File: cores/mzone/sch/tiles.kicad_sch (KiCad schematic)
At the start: 37 parts

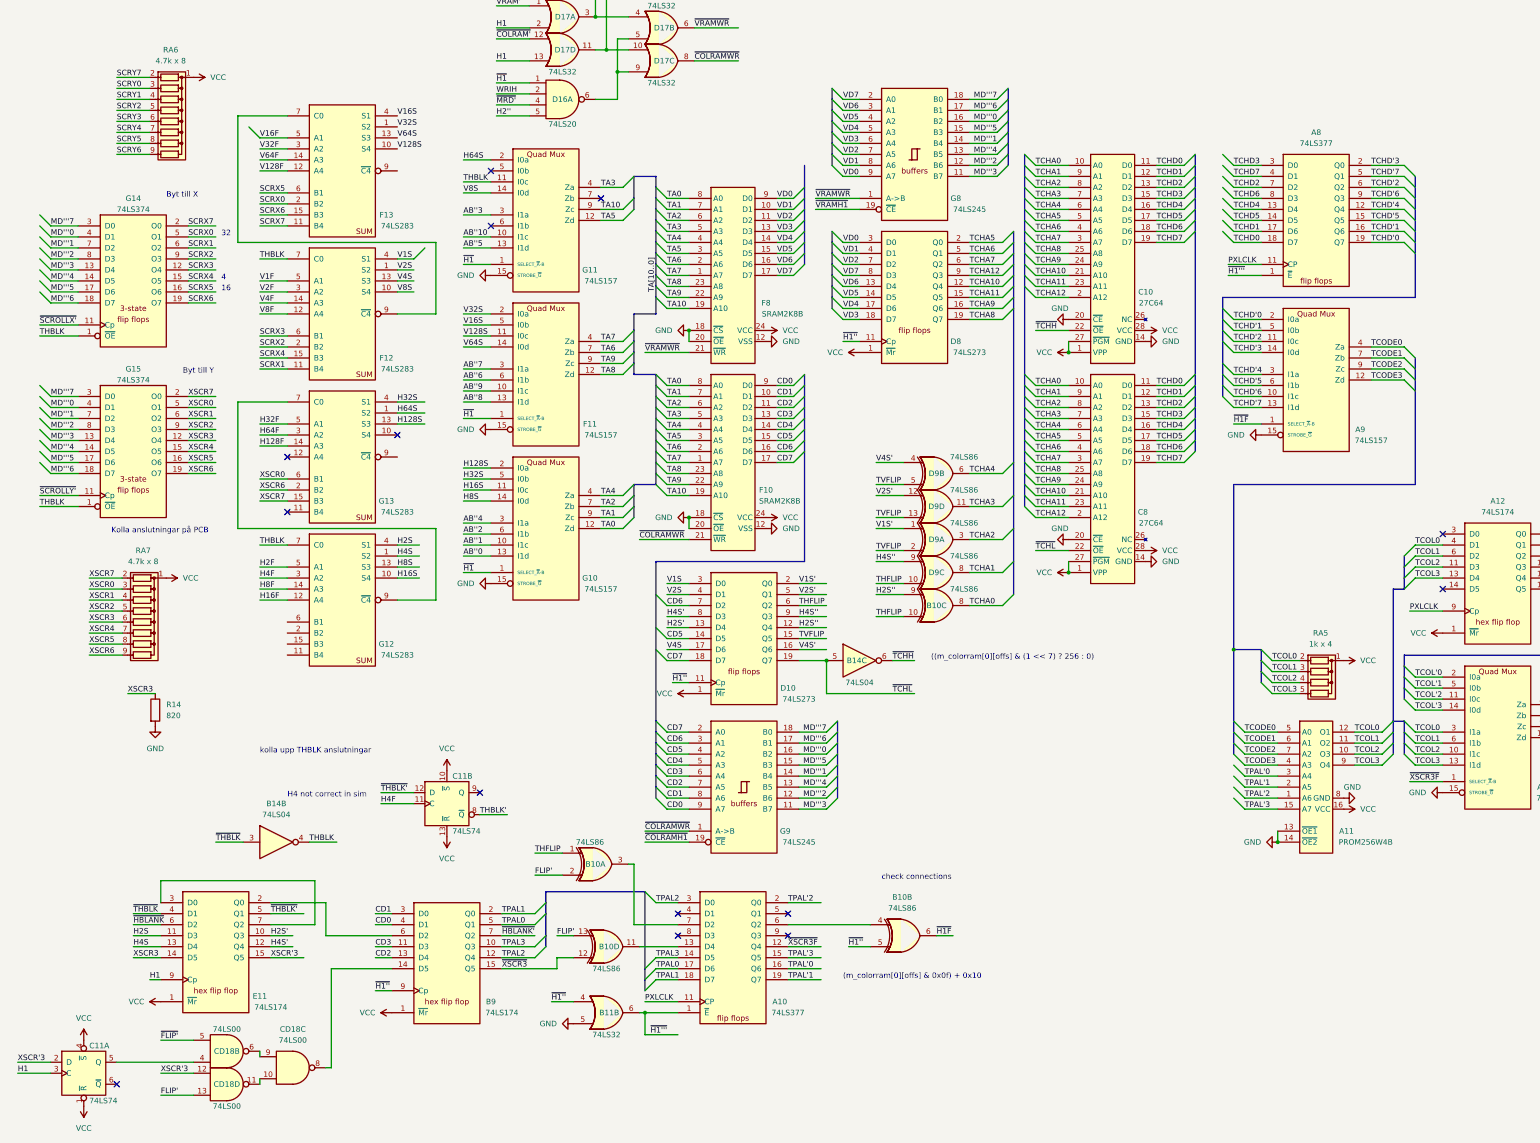
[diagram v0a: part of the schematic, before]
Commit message: mzone sim working, no sound.
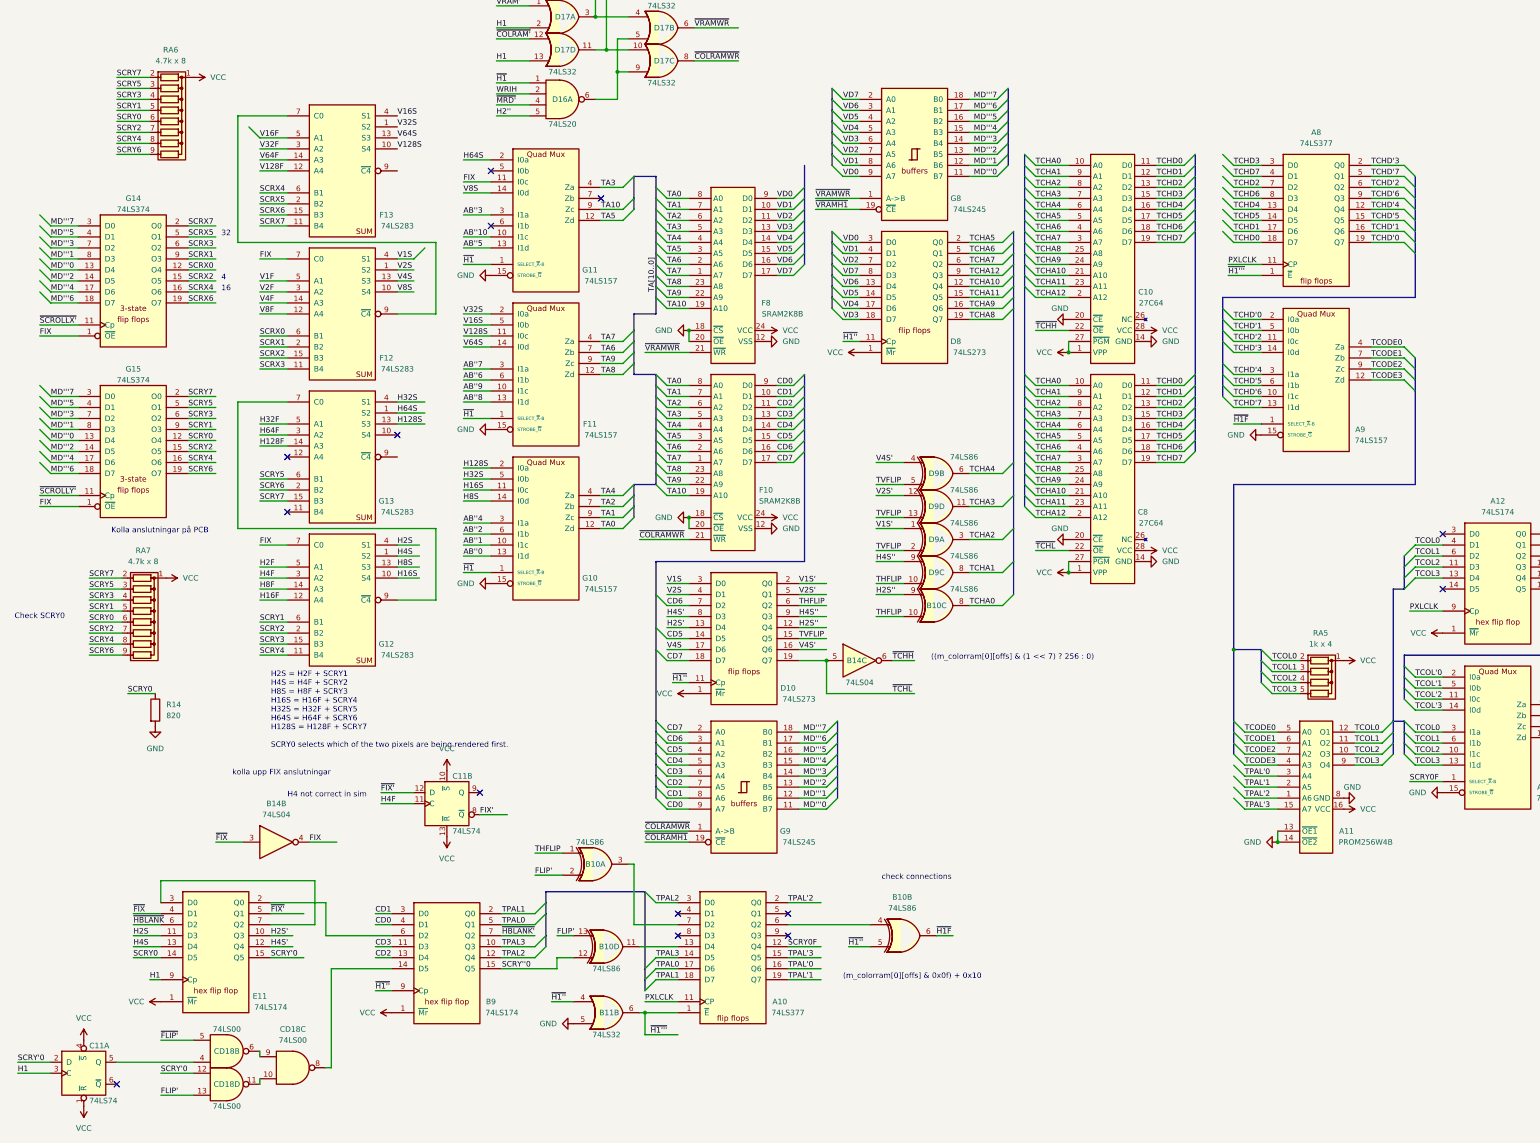
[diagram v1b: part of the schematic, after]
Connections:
- net XSCR0 is gone; now on net SCRY5: G13.6 (B1), G15.5 (O1), RA7.3 (R2)
- net XSCR1 is gone; now on net SCRY3: G15.6 (O2), RA7.4 (R3)
- net XSCR2 is gone; now on net SCRY1: G15.9 (O3), RA7.5 (R4)
- net XSCR3 is gone; now on net SCRY0: E11.14 (D5), G15.12 (O4), R14.1, RA7.6 (R5)
- net XSCR4 is gone; now on net SCRY2: G15.15 (O5), RA7.7 (R6)
- net XSCR5 is gone; now on net SCRY4: G15.16 (O6), RA7.8 (R7)
- net XSCR6 is gone; now on net SCRY6: G13.2 (B2), G15.19 (O7), RA7.9 (R8)
- net XSCR7 is gone; now on net SCRY7: G13.15 (B3), G15.2 (O0), RA7.2 (R1)
- net MD'''0: now also G14.13 (D4), G15.13 (D4), G8.11 (B7), G9.11 (B7); no longer G14.4 (D1), G15.4 (D1), G8.16 (B2), G9.16 (B2)
- net MD'''1: now also G14.8 (D3), G15.8 (D3), G8.12 (B6), G9.12 (B6); no longer G14.7 (D2), G15.7 (D2), G8.14 (B4), G9.14 (B4)
- net MD'''2: now also G14.14 (D5), G15.14 (D5), G8.13 (B5), G9.13 (B5); no longer G14.8 (D3), G15.8 (D3), G8.12 (B6), G9.12 (B6)
- net MD'''3: now also G14.7 (D2), G15.7 (D2), G8.14 (B4), G9.14 (B4); no longer G14.13 (D4), G15.13 (D4), G8.11 (B7), G9.11 (B7)
- net MD'''4: now also G14.17 (D6), G15.17 (D6), G8.15 (B3), G9.15 (B3); no longer G14.14 (D5), G15.14 (D5), G8.13 (B5), G9.13 (B5)
- net MD'''5: now also G14.4 (D1), G15.4 (D1), G8.16 (B2), G9.16 (B2); no longer G14.17 (D6), G15.17 (D6), G8.15 (B3), G9.15 (B3)
- net SCRX0: now also F12.6 (B1), G14.12 (O4); no longer F13.2 (B2), G14.5 (O1)
- net SCRX1: now also F12.2 (B2), G14.9 (O3); no longer F12.11 (B4), G14.6 (O2)
- net SCRX2: now also F12.15 (B3), G14.15 (O5); no longer F12.2 (B2), G14.9 (O3)
- net SCRX3: now also F12.11 (B4), G14.6 (O2); no longer F12.6 (B1), G14.12 (O4)
- net SCRX4: now also F13.6 (B1), G14.16 (O6); no longer F12.15 (B3), G14.15 (O5)
- net SCRX5: now also F13.2 (B2), G14.5 (O1); no longer F13.6 (B1), G14.16 (O6)
- net SCRY0: now also RA6.6 (R5); no longer RA6.3 (R2)
- net SCRY1: now also G12.6 (B1), RA6.5 (R4); no longer RA6.4 (R3)
- net SCRY2: now also G12.2 (B2), RA6.7 (R6); no longer RA6.5 (R4)
- net SCRY3: now also G12.15 (B3), RA6.4 (R3); no longer RA6.6 (R5)
- net SCRY4: now also G12.11 (B4), RA6.8 (R7); no longer RA6.7 (R6)
- net SCRY5: now also RA6.3 (R2); no longer RA6.8 (R7)
- net THBLK renamed FIX
- net THBLK' renamed FIX'
- net XSCR'3 renamed SCRY'0
- net ~{THBLK'} renamed ~{FIX'}
- net ~{THBLK} renamed ~{FIX}
- net ~{XSCR3F} renamed SCRY0F
- net ~{XSCR3} renamed SCRY''0
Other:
- note added: "Check SCRY0"
- note added: "H2S = H2F + SCRY1 H4S = H4F + SCRY2 H8S = H8F + SCRY3 H16S = H16F + SCRY4 H32S = H32F + SCRY5 H64S = H64F + SCRY6 H128S = H128F + SCRY7 SCRY0 selects which of the two pixels are being rendered first."
- note added: "kolla upp FIX anslutningar"
- note removed: "Byt till X"
- note removed: "Byt till Y"
- note removed: "kolla upp THBLK anslutningar"

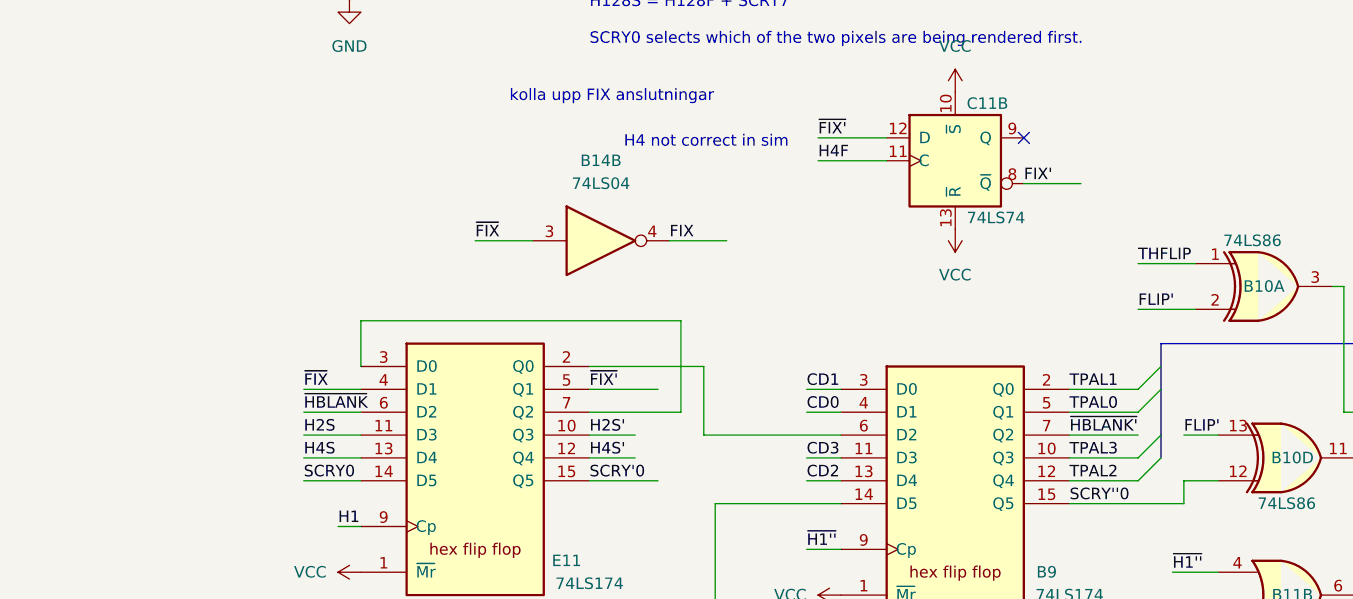
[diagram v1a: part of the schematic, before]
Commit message: mzone core
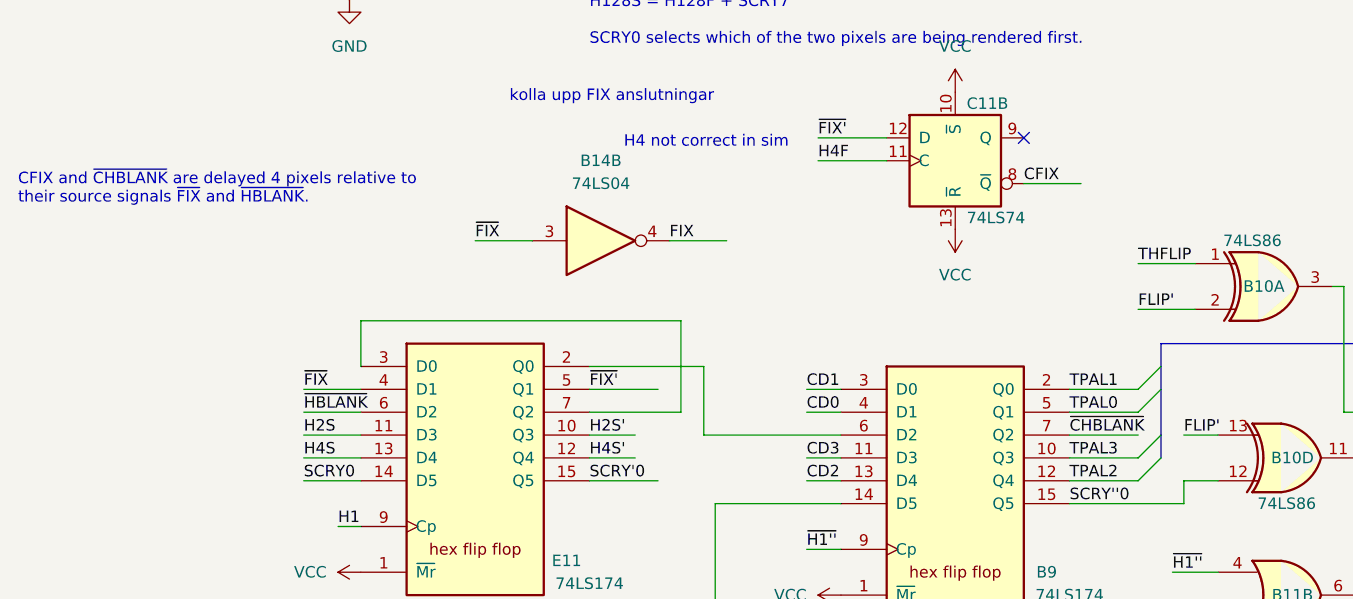
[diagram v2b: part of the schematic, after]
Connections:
- net FIX' renamed CFIX
- net ~{HBLANK'} renamed ~{CHBLANK}
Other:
- note added: "CFIX and ~{CHBLANK} are delayed 4 pixels relative to their source signals ~{FIX} and ~{HBLANK}."
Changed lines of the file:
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@@
+		)
+	)
+	(text "CFIX and ~{CHBLANK} are delayed 4 pixels relative to\ntheir source signals ~{FIX} and ~{HBLANK}."
+		(exclude_from_sim no)
+		(at 13.97 210.185 0)
+		(effects
+			(font
+				(size 1.27 1.27)
+			)
+			(justify left)
 		)
 	)
@@
 		)
 	)
-	(label "FIX'"
+	(label "CFIX"
 		(at 125.73 209.55 0)
 		(fields_autoplaced yes)
@@
 		)
 	)
-	(label "~{HBLANK'}"
+	(label "~{CHBLANK}"
 		(at 130.81 237.49 0)
 		(fields_autoplaced yes)

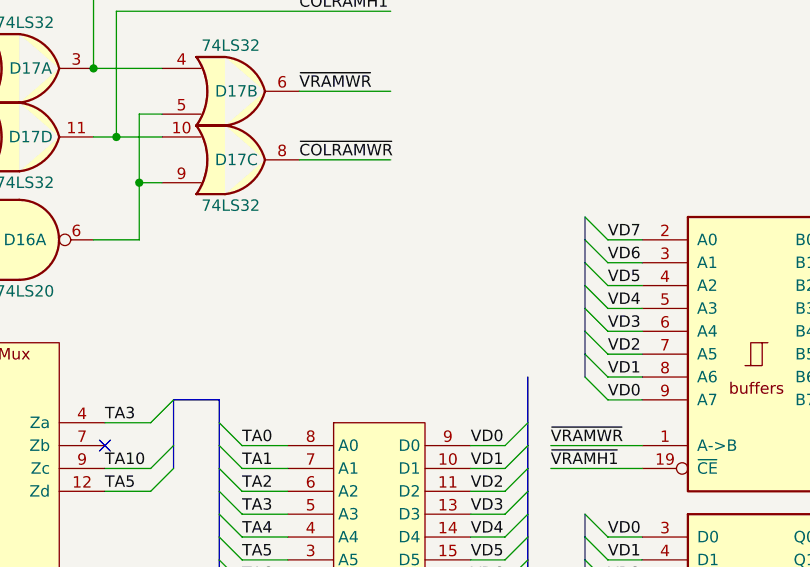
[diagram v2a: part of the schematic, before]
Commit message: mzone core
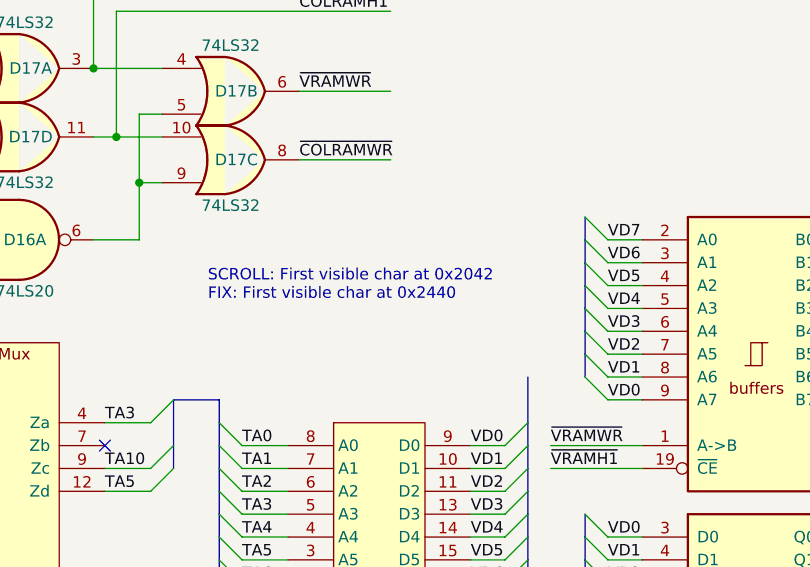
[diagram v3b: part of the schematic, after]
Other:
- note added: "SCROLL: First visible char at 0x2042 FIX: First visible char at 0x2440"

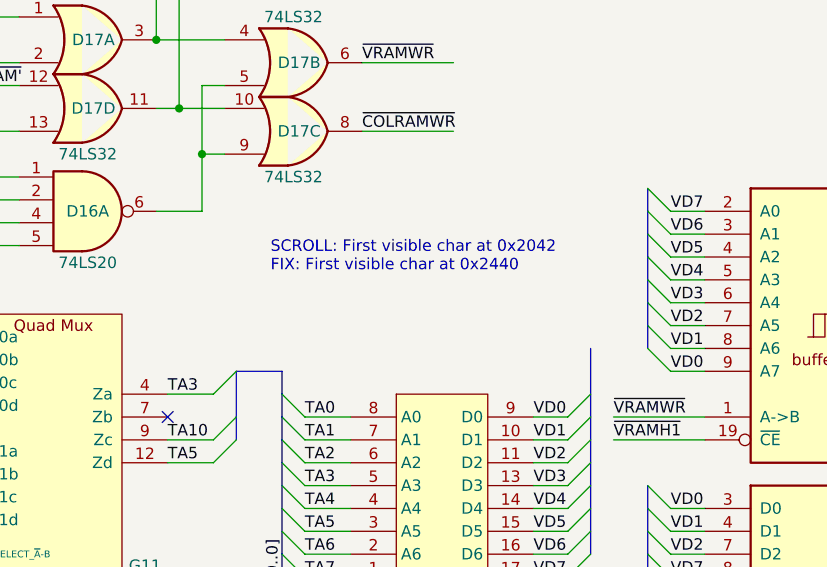
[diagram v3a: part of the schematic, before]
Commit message: mzone core
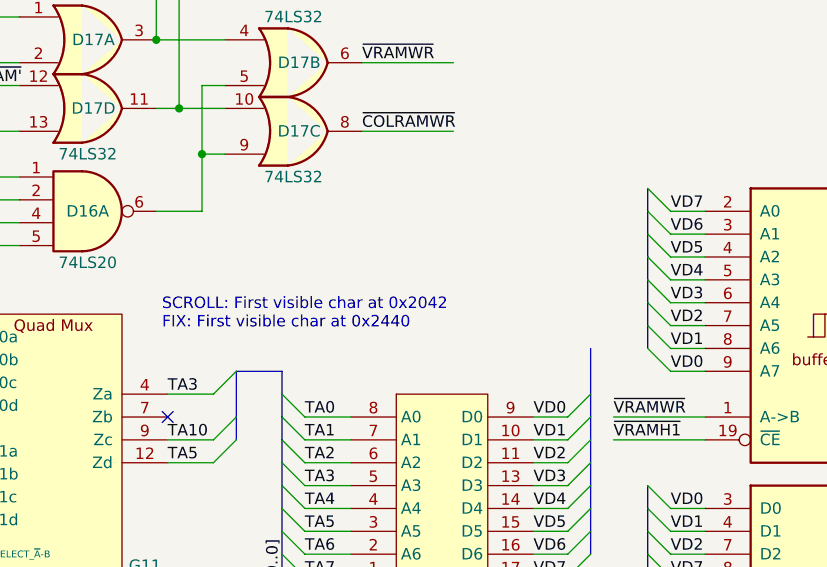
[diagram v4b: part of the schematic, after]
